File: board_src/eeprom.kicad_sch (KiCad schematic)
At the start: 4 parts, among them IC2 M93C46-WMN6TP, U2 AT24CS04-SSHM

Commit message: Wersja początkowa 9.0
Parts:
- removed IC2: M93C46-WMN6TP, SOIC127P600X175-8N, symbol M93C46-WMN6TP:M93C46-WMN6TP
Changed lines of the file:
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@@
-	)
-	(symbol
-		(lib_id "M93C46-WMN6TP:M93C46-WMN6TP")
-		(at 138.43 91.44 0)
-		(unit 1)
-		(exclude_from_sim no)
-		(in_bom yes)
-		(on_board yes)
-		(dnp no)
-		(fields_autoplaced yes)
-		(property "Reference" "IC2"
-			(at 149.86 83.82 0)
-			(effects
-				(font
-					(size 1.27 1.27)
-				)
-			)
-		)
-		(property "Value" "M93C46-WMN6TP"
-			(at 149.86 86.36 0)
-			(effects
-				(font
-					(size 1.27 1.27)
-				)
-			)
-		)
-		(property "Footprint" "SOIC127P600X175-8N"
-			(at 157.48 186.36 0)
-			(effects
-				(font
-					(size 1.27 1.27)
-				)
-				(justify left top)
-				(hide yes)
-			)
-		)
-		(property "Datasheet" "http://www.st.com/st-web-ui/static/active/en/resource/technical/document/datasheet/CD00001142.pdf"
-			(at 157.48 286.36 0)
-			(effects
-				(font
-					(size 1.27 1.27)
-				)
-				(justify left top)
-				(hide yes)
-			)
-		)
-		(property "Description" "M93C46-WMN6TP, Serial EEPROM Memory 1kbit, Serial-Microwire, 200ns 2.5  5.5 V, 8-Pin SOIC"
-			(at 138.43 91.44 0)
-			(effects
-				(font
-					(size 1.27 1.27)
-				)
-				(hide yes)
-			)
-		)
-		(property "Height" "1.75"
-			(at 157.48 486.36 0)
-			(effects
-				(font
-					(size 1.27 1.27)
-				)
-				(justify left top)
-				(hide yes)
-			)
-		)
-		(property "TME Electronic Components Part Number" ""
-			(at 157.48 586.36 0)
-			(effects
-				(font
-					(size 1.27 1.27)
-				)
-				(justify left top)
-				(hide yes)
-			)
-		)
-		(property "TME Electronic Components Price/Stock" ""
-			(at 157.48 686.36 0)
-			(effects
-				(font
-					(size 1.27 1.27)
-				)
-				(justify left top)
-				(hide yes)
-			)
-		)
-		(property "Manufacturer_Name" "STMicroelectronics"
-			(at 157.48 786.36 0)
-			(effects
-				(font
-					(size 1.27 1.27)
-				)
-				(justify left top)
-				(hide yes)
-			)
-		)
-		(property "Manufacturer_Part_Number" "M93C46-WMN6TP"
-			(at 157.48 886.36 0)
-			(effects
-				(font
-					(size 1.27 1.27)
-				)
-				(justify left top)
-				(hide yes)
-			)
-		)
-		(pin "5"
-		)
-		(pin "8"
-		)
-		(pin "2"
-		)
-		(pin "3"
-		)
-		(pin "1"
-		)
-		(pin "6"
-		)
-		(pin "7"
-		)
-		(pin "4"
-		)
-		(instances
-			(project "board"
-				(path "/772e9f49-cfcf-4cf6-843d-0684684f2d4b/8b8e205f-8cd6-4f90-881c-a100662c7649"
-					(reference "IC2")
-					(unit 1)
-				)
-			)
-		)
 	)
 	(symbol

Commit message: wersja dodane arkusze hierarchiczne
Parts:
- removed R1, R2: 10k, Resistor_SMD:R_0201_0603Metric, symbol Device:R
- removed U2: AT24CS04-SSHM, Package_SO:SOIC-8_3.9x4.9mm_P1.27mm, symbol Memory_EEPROM:AT24CS04-SSHM
- added IC2: M24C02-WMN6TP, SOIC127P600X175-8N, symbol M24C02-WMN6TP:M24C02-WMN6TP
- added J10: Conn_01x01_Pin, symbol Connector:Conn_01x01_Pin
- added R15, R16: 10k, Resistor_SMD:R_0201_0603Metric, symbol Device:R
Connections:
- new net: IC2.6 (SCL), R15.1
- new net: IC2.7 (~{WC}), J10.1 (Pin_1)
- new net: IC2.5 (SDA), R16.1
- new net 3,3V: IC2.8 (VCC), R15.2, R16.2
- new net gnd: IC2.1 (E0), IC2.2 (E1), IC2.3 (E2), IC2.4 (VSS)
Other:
- note added: "czy chcemy mieć możliwość zapisu do eeprom?"
- note removed: "EEPROM"

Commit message: wersja dodane arkusze hierarchiczne
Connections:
- net 3,3V renamed +3.3V
- net gnd renamed GND
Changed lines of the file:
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@@
-	)
-	(junction
-		(at 180.34 92.71)
-		(diameter 0)
-		(color 0 0 0 0)
 	)
 	(junction
@@
 	(wire
 		(pts
-			(xy 176.53 92.71) (xy 180.34 92.71)
+			(xy 180.34 92.71) (xy 187.96 92.71)
 		)
 		(stroke
@@
 	(wire
 		(pts
-			(xy 208.28 97.79) (xy 213.36 97.79)
+			(xy 208.28 97.79) (xy 214.63 97.79)
 		)
 		(stroke
@@
 	(wire
 		(pts
-			(xy 147.32 114.3) (xy 149.86 114.3)
-		)
-		(stroke
-			(width 0)
-			(type default)
-		)
-	)
-	(wire
-		(pts
 			(xy 200.66 97.79) (xy 208.28 97.79)
 		)
@@
 	(wire
 		(pts
-			(xy 180.34 92.71) (xy 187.96 92.71)
-		)
-		(stroke
-			(width 0)
-			(type default)
-		)
-	)
-	(wire
-		(pts
 			(xy 149.86 92.71) (xy 154.94 92.71)
 		)
@@
 		)
 	)
-	(global_label "gnd"
-		(shape passive)
-		(at 147.32 114.3 180)
+	(symbol
+		(lib_id "power:GND")
+		(at 149.86 114.3 0)
+		(unit 1)
+		(exclude_from_sim no)
+		(in_bom yes)
+		(on_board yes)
+		(dnp no)
 		(fields_autoplaced yes)
-		(effects
-			(font
-				(size 1.27 1.27)
-			)
-			(justify right)
-		)
-		(property "Intersheetrefs" "${INTERSHEET_REFS}"
-			(at 141.9991 114.3 0)
-			(effects
-				(font
-					(size 1.27 1.27)
-				)
-				(justify right)
-				(hide yes)
-			)
-		)
-	)
-	(global_label "3,3V"
-		(shape passive)
-		(at 213.36 97.79 0)
-		(fields_autoplaced yes)
-		(effects
-			(font
-				(size 1.27 1.27)
-			)
-			(justify left)
-		)
-		(property "Intersheetrefs" "${INTERSHEET_REFS}"
-			(at 219.3463 97.79 0)
-			(effects
-				(font
-					(size 1.27 1.27)
-				)
-				(justify left)
-				(hide yes)
+		(property "Reference" "#PWR017"
+			(at 149.86 120.65 0)
+			(effects
+				(font
+					(size 1.27 1.27)
+				)
+				(hide yes)
+			)
+		)
+		(property "Value" "GND"
+			(at 149.86 119.38 0)
+			(effects
+				(font
+					(size 1.27 1.27)
+				)
+			)
+		)
+		(property "Footprint" ""
+			(at 149.86 114.3 0)
+			(effects
+				(font
+					(size 1.27 1.27)
+				)
+				(hide yes)
+			)
+		)
+		(property "Datasheet" ""
+			(at 149.86 114.3 0)
+			(effects
+				(font
+					(size 1.27 1.27)
+				)
+				(hide yes)
+			)
+		)
+		(property "Description" "Power symbol creates a global label with name \"GND\" , ground"
+			(at 149.86 114.3 0)
+			(effects
+				(font
+					(size 1.27 1.27)
+				)
+				(hide yes)
+			)
+		)
+		(pin "1"
+		)
+		(instances
+			(project ""
+				(path "/772e9f49-cfcf-4cf6-843d-0684684f2d4b/8b8e205f-8cd6-4f90-881c-a100662c7649"
+					(reference "#PWR017")
+					(unit 1)
+				)
 			)
 		)
@@
 					(unit 1)
 				)
+			)
+		)
+	)
+	(symbol
+		(lib_id "power:+3.3V")
+		(at 214.63 97.79 270)
+		(unit 1)
+		(exclude_from_sim no)
+		(in_bom yes)
+		(on_board yes)
+		(dnp no)
+		(fields_autoplaced yes)
+		(property "Reference" "#PWR010"
+			(at 210.82 97.79 0)
+			(effects
+				(font
+					(size 1.27 1.27)
+				)
+				(hide yes)
+			)
+		)
+		(property "Value" "+3.3V"
+			(at 218.44 97.7899 90)
+			(effects
+				(font
+					(size 1.27 1.27)
+				)
+				(justify left)
+			)
+		)
+		(property "Footprint" ""
+			(at 214.63 97.79 0)
+			(effects
+				(font
+					(size 1.27 1.27)
+				)
+				(hide yes)
+			)
+		)
+		(property "Datasheet" ""
+			(at 214.63 97.79 0)
+			(effects
+				(font
+					(size 1.27 1.27)
+				)
+				(hide yes)
+			)
+		)
+		(property "Description" "Power symbol creates a global label with name \"+3.3V\""
+			(at 214.63 97.79 0)
+			(effects
+				(font
+					(size 1.27 1.27)
+				)
+				(hide yes)
+			)
+		)
+		(pin "1"
+		)
+		(instances
+			(project "board"
+				(path "/772e9f49-cfcf-4cf6-843d-0684684f2d4b/8b8e205f-8cd6-4f90-881c-a100662c7649"
+					(reference "#PWR010")
+					(unit 1)
+				)

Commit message: wersja uzupelnione footprinty
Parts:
- IC2: footprint SOIC127P600X175-8N -> footprints:EEPROM
- J10: footprint (none) -> Connector_PinHeader_2.54mm:PinHeader_1x01_P2.54mm_Vertical
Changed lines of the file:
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@@
 			)
 		)
-		(property "Footprint" ""
+		(property "Footprint" "Connector_PinHeader_2.54mm:PinHeader_1x01_P2.54mm_Vertical"
 			(at 193.04 92.71 0)
 			(effects
@@
 			)
 		)
-		(property "Footprint" "SOIC127P600X175-8N"
+		(property "Footprint" "footprints:EEPROM"
 			(at 176.53 185.09 0)
 			(effects

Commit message: wersja 3d
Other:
- note added: "Jaka wartość oporników?"
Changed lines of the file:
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@@
 	(generator_version "9.0")
 	(paper "A4")
+	(text "Jaka wartość oporników?\n"
+		(exclude_from_sim no)
+		(at 193.548 113.284 0)
+		(effects
+			(font
+				(size 1.27 1.27)
+			)
+		)
+	)
 	(text "czy chcemy mieć możliwość zapisu do eeprom?"
 		(exclude_from_sim no)

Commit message: uporzadkowane 3D
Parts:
- added J19, J28: Conn_01x01_Pin, Connector_PinHeader_2.54mm:PinHeader_1x01_P2.54mm_Vertical, symbol Connector:Conn_01x01_Pin
- R15, R16: value 10k -> 4.7k
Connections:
- net +3.3V: no longer R15.2, R16.2
- new net: J28.1 (Pin_1), R16.2
- new net: J19.1 (Pin_1), R15.2
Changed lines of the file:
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@@
-	)
-	(junction
-		(at 208.28 97.79)
-		(diameter 0)
-		(color 0 0 0 0)
 	)
 	(junction
@@
 		(color 0 0 0 0)
 	)
-	(junction
-		(at 200.66 97.79)
-		(diameter 0)
-		(color 0 0 0 0)
+	(wire
+		(pts
+			(xy 205.74 102.87) (xy 205.74 100.33)
+		)
+		(stroke
+			(width 0)
+			(type default)
+		)
 	)
 	(wire
@@
 	(wire
 		(pts
-			(xy 196.85 97.79) (xy 200.66 97.79)
-		)
-		(stroke
-			(width 0)
-			(type default)
-		)
-	)
-	(wire
-		(pts
 			(xy 149.86 92.71) (xy 149.86 95.25)
 		)
@@
 	(wire
 		(pts
-			(xy 185.42 85.09) (xy 208.28 85.09)
+			(xy 185.42 85.09) (xy 214.63 85.09)
 		)
 		(stroke
@@
 	(wire
 		(pts
-			(xy 208.28 97.79) (xy 214.63 97.79)
-		)
-		(stroke
-			(width 0)
-			(type default)
-		)
-	)
-	(wire
-		(pts
 			(xy 149.86 97.79) (xy 149.86 114.3)
 		)
@@
 	(wire
 		(pts
-			(xy 196.85 97.79) (xy 196.85 102.87)
-		)
-		(stroke
-			(width 0)
-			(type default)
-		)
-	)
-	(wire
-		(pts
-			(xy 200.66 97.79) (xy 208.28 97.79)
+			(xy 196.85 102.87) (xy 205.74 102.87)
 		)
 		(stroke
@@
 	(wire
 		(pts
-			(xy 196.85 105.41) (xy 200.66 105.41)
-		)
-		(stroke
-			(width 0)
-			(type default)
-		)
-	)
-	(wire
-		(pts
-			(xy 200.66 97.79) (xy 200.66 105.41)
-		)
-		(stroke
-			(width 0)
-			(type default)
-		)
-	)
-	(wire
-		(pts
-			(xy 208.28 85.09) (xy 208.28 97.79)
+			(xy 196.85 105.41) (xy 205.74 105.41)
 		)
 		(stroke
@@
 		(pts
 			(xy 149.86 90.17) (xy 149.86 92.71)
+		)
+		(stroke
+			(width 0)
+			(type default)
+		)
+	)
+	(wire
+		(pts
+			(xy 205.74 105.41) (xy 205.74 106.68)
 		)
 		(stroke
@@
 	)
 	(symbol
+		(lib_id "Connector:Conn_01x01_Pin")
+		(at 210.82 106.68 180)
+		(unit 1)
+		(exclude_from_sim no)
+		(in_bom yes)
+		(on_board yes)
+		(dnp no)
+		(property "Reference" "J28"
+			(at 211.074 104.902 0)
+			(effects
+				(font
+					(size 1.27 1.27)
+				)
+			)
+		)
+		(property "Value" "Conn_01x01_Pin"
+			(at 219.964 106.426 0)
+			(effects
+				(font
+					(size 1.27 1.27)
+				)
+			)
+		)
+		(property "Footprint" "Connector_PinHeader_2.54mm:PinHeader_1x01_P2.54mm_Vertical"
+			(at 210.82 106.68 0)
+			(effects
+				(font
+					(size 1.27 1.27)
+				)
+				(hide yes)
+			)
+		)
+		(property "Datasheet" "~"
+			(at 210.82 106.68 0)
+			(effects
+				(font
+					(size 1.27 1.27)
+				)
+				(hide yes)
+			)
+		)
+		(property "Description" "Generic connector, single row, 01x01, script generated"
+			(at 210.82 106.68 0)
+			(effects
+				(font
+					(size 1.27 1.27)
+				)
+				(hide yes)
+			)
+		)
+		(pin "1"
+		)
+		(instances
+			(project "board"
+				(path "/772e9f49-cfcf-4cf6-843d-0684684f2d4b/8b8e205f-8cd6-4f90-881c-a100662c7649"
+					(reference "J28")
+					(unit 1)
+				)
+			)
+		)
+	)
+	(symbol
 		(lib_id "Device:R")
 		(at 193.04 102.87 90)
@@
 			)
 		)
-		(property "Value" "10k"
+		(property "Value" "4.7k"
 			(at 193.04 99.06 90)
 			(effects
@@
 	(symbol
 		(lib_id "power:+3.3V")
-		(at 214.63 97.79 270)
+		(at 214.63 85.09 270)
 		(unit 1)
 		(exclude_from_sim no)
@@
 		(on_board yes)
 		(dnp no)
-		(fields_autoplaced yes)
 		(property "Reference" "#PWR010"
-			(at 210.82 97.79 0)
+			(at 210.82 85.09 0)
 			(effects
 				(font
@@
 		)
 		(property "Value" "+3.3V"
-			(at 218.44 97.7899 90)
+			(at 217.678 85.09 90)
 			(effects
 				(font
@@
 		)
 		(property "Footprint" ""
-			(at 214.63 97.79 0)
+			(at 214.63 85.09 0)
 			(effects
 				(font
@@
 		)
 		(property "Datasheet" ""
-			(at 214.63 97.79 0)
+			(at 214.63 85.09 0)
 			(effects
 				(font
@@
 		)
 		(property "Description" "Power symbol creates a global label with name \"+3.3V\""
-			(at 214.63 97.79 0)
+			(at 214.63 85.09 0)
 			(effects
 				(font
@@
 				(path "/772e9f49-cfcf-4cf6-843d-0684684f2d4b/8b8e205f-8cd6-4f90-881c-a100662c7649"
 					(reference "J10")
+					(unit 1)
+				)
+			)
+		)
+	)
+	(symbol
+		(lib_id "Connector:Conn_01x01_Pin")
+		(at 210.82 100.33 180)
+		(unit 1)
+		(exclude_from_sim no)
+		(in_bom yes)
+		(on_board yes)
+		(dnp no)
+		(property "Reference" "J19"
+			(at 211.328 99.06 0)
+			(effects
+				(font
+					(size 1.27 1.27)
+				)
+			)
+		)
+		(property "Value" "Conn_01x01_Pin"
+			(at 220.726 100.33 0)
+			(effects
+				(font
+					(size 1.27 1.27)
+				)
+			)
+		)
+		(property "Footprint" "Connector_PinHeader_2.54mm:PinHeader_1x01_P2.54mm_Vertical"
+			(at 210.82 100.33 0)
+			(effects
+				(font
+					(size 1.27 1.27)
+				)
+				(hide yes)
+			)
+		)
+		(property "Datasheet" "~"
+			(at 210.82 100.33 0)
+			(effects
+				(font
+					(size 1.27 1.27)
+				)
+				(hide yes)
+			)
+		)
+		(property "Description" "Generic connector, single row, 01x01, script generated"
+			(at 210.82 100.33 0)
+			(effects
+				(font
+					(size 1.27 1.27)
+				)
+				(hide yes)
+			)
+		)
+		(pin "1"
+		)
+		(instances
+			(project ""
+				(path "/772e9f49-cfcf-4cf6-843d-0684684f2d4b/8b8e205f-8cd6-4f90-881c-a100662c7649"
+					(reference "J19")
 					(unit 1)
 				)
@@
 			)
 		)
-		(property "Value" "10k"
+		(property "Value" "4.7k"
 			(at 193.04 109.474 90)
 			(effects

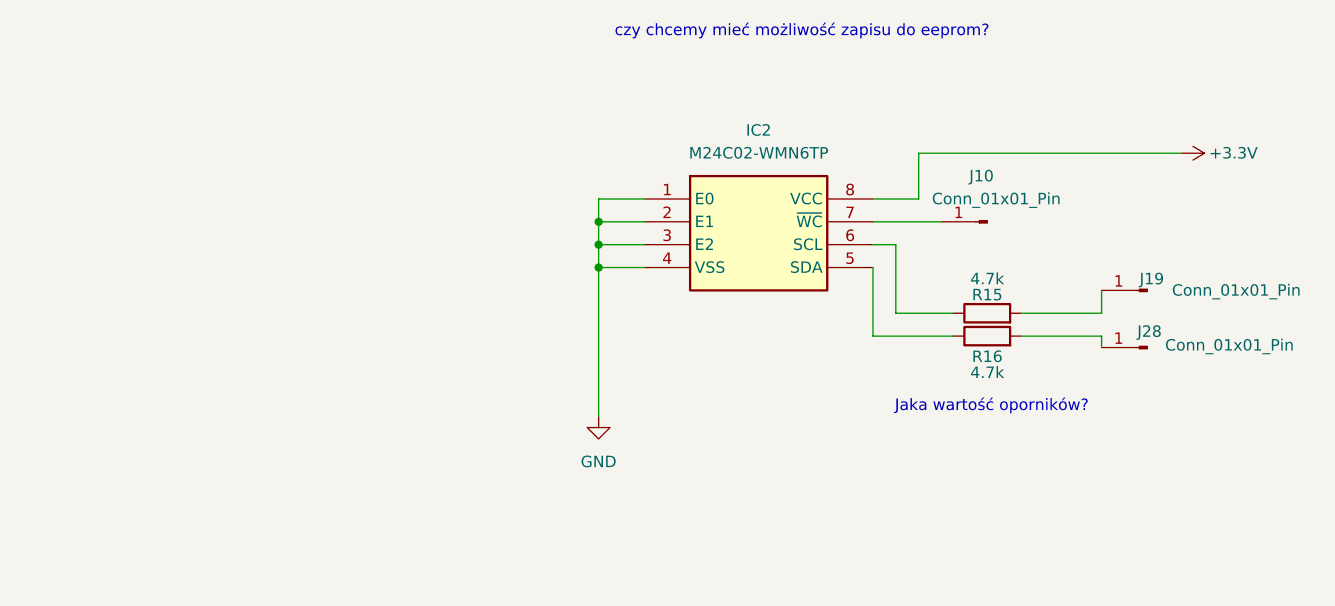
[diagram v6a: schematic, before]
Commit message: wersja z wyswietlaczem LCD
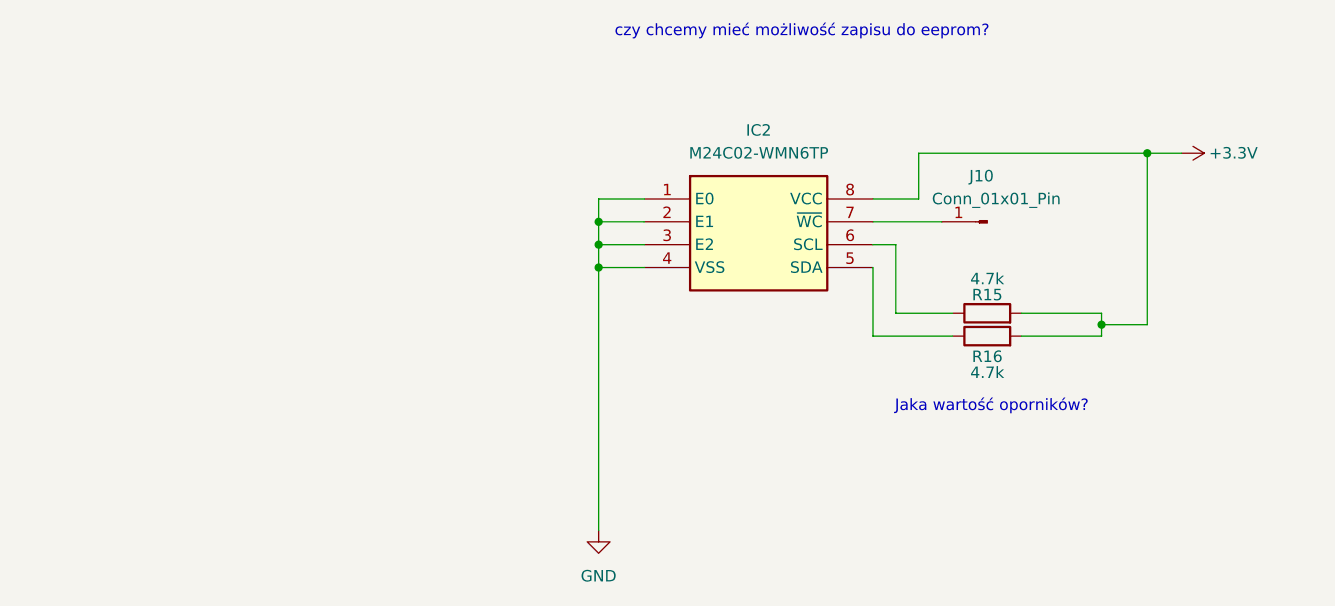
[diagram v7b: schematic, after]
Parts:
- removed J19, J28: Conn_01x01_Pin, Connector_PinHeader_2.54mm:PinHeader_1x01_P2.54mm_Vertical, symbol Connector:Conn_01x01_Pin
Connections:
- net +3.3V: now also R15.2, R16.2
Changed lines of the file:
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@@
+	)
+	(junction
+		(at 205.74 104.14)
+		(diameter 0)
+		(color 0 0 0 0)
 	)
 	(junction
@@
 		(color 0 0 0 0)
 	)
-	(wire
-		(pts
-			(xy 205.74 102.87) (xy 205.74 100.33)
-		)
-		(stroke
-			(width 0)
-			(type default)
-		)
+	(junction
+		(at 210.82 85.09)
+		(diameter 0)
+		(color 0 0 0 0)
 	)
 	(wire
@@
 	(wire
 		(pts
+			(xy 205.74 104.14) (xy 210.82 104.14)
+		)
+		(stroke
+			(width 0)
+			(type default)
+		)
+	)
+	(wire
+		(pts
+			(xy 210.82 104.14) (xy 210.82 85.09)
+		)
+		(stroke
+			(width 0)
+			(type default)
+		)
+	)
+	(wire
+		(pts
+			(xy 205.74 102.87) (xy 205.74 104.14)
+		)
+		(stroke
+			(width 0)
+			(type default)
+		)
+	)
+	(wire
+		(pts
 			(xy 149.86 92.71) (xy 149.86 95.25)
 		)
@@
 	(wire
 		(pts
-			(xy 185.42 85.09) (xy 214.63 85.09)
+			(xy 185.42 85.09) (xy 210.82 85.09)
 		)
 		(stroke
@@
 	(wire
 		(pts
-			(xy 149.86 97.79) (xy 149.86 114.3)
+			(xy 149.86 97.79) (xy 149.86 127)
 		)
 		(stroke
@@
 	(wire
 		(pts
+			(xy 205.74 104.14) (xy 205.74 105.41)
+		)
+		(stroke
+			(width 0)
+			(type default)
+		)
+	)
+	(wire
+		(pts
 			(xy 182.88 102.87) (xy 189.23 102.87)
 		)
@@
 	(wire
 		(pts
+			(xy 210.82 85.09) (xy 214.63 85.09)
+		)
+		(stroke
+			(width 0)
+			(type default)
+		)
+	)
+	(wire
+		(pts
 			(xy 196.85 105.41) (xy 205.74 105.41)
 		)
@@
 		(pts
 			(xy 149.86 90.17) (xy 149.86 92.71)
-		)
-		(stroke
-			(width 0)
-			(type default)
-		)
-	)
-	(wire
-		(pts
-			(xy 205.74 105.41) (xy 205.74 106.68)
 		)
 		(stroke
@@
 	(symbol
 		(lib_id "power:GND")
-		(at 149.86 114.3 0)
+		(at 149.86 127 0)
 		(unit 1)
 		(exclude_from_sim no)
@@
 		(fields_autoplaced yes)
 		(property "Reference" "#PWR017"
-			(at 149.86 120.65 0)
+			(at 149.86 133.35 0)
 			(effects
 				(font
@@
 		)
 		(property "Value" "GND"
-			(at 149.86 119.38 0)
+			(at 149.86 132.08 0)
 			(effects
 				(font
@@
 		)
 		(property "Footprint" ""
-			(at 149.86 114.3 0)
+			(at 149.86 127 0)
 			(effects
 				(font
@@
 		)
 		(property "Datasheet" ""
-			(at 149.86 114.3 0)
+			(at 149.86 127 0)
 			(effects
 				(font
@@
 		)
 		(property "Description" "Power symbol creates a global label with name \"GND\" , ground"
-			(at 149.86 114.3 0)
+			(at 149.86 127 0)
 			(effects
 				(font
@@
 				(path "/772e9f49-cfcf-4cf6-843d-0684684f2d4b/8b8e205f-8cd6-4f90-881c-a100662c7649"
 					(reference "#PWR017")
-					(unit 1)
-				)
-			)
-		)
-	)
-	(symbol
-		(lib_id "Connector:Conn_01x01_Pin")
-		(at 210.82 106.68 180)
-		(unit 1)
-		(exclude_from_sim no)
-		(in_bom yes)
-		(on_board yes)
-		(dnp no)
-		(property "Reference" "J28"
-			(at 211.074 104.902 0)
-			(effects
-				(font
-					(size 1.27 1.27)
-				)
-			)
-		)
-		(property "Value" "Conn_01x01_Pin"
-			(at 219.964 106.426 0)
-			(effects
-				(font
-					(size 1.27 1.27)
-				)
-			)
-		)
-		(property "Footprint" "Connector_PinHeader_2.54mm:PinHeader_1x01_P2.54mm_Vertical"
-			(at 210.82 106.68 0)
-			(effects
-				(font
-					(size 1.27 1.27)
-				)
-				(hide yes)
-			)
-		)
-		(property "Datasheet" "~"
-			(at 210.82 106.68 0)
-			(effects
-				(font
-					(size 1.27 1.27)
-				)
-				(hide yes)
-			)
-		)
-		(property "Description" "Generic connector, single row, 01x01, script generated"
-			(at 210.82 106.68 0)
-			(effects
-				(font
-					(size 1.27 1.27)
-				)
-				(hide yes)
-			)
-		)
-		(pin "1"
-		)
-		(instances
-			(project "board"
-				(path "/772e9f49-cfcf-4cf6-843d-0684684f2d4b/8b8e205f-8cd6-4f90-881c-a100662c7649"
-					(reference "J28")
 					(unit 1)
 				)
@@
 					(unit 1)
 				)
-			)
-		)
-	)
-	(symbol
-		(lib_id "Connector:Conn_01x01_Pin")
-		(at 210.82 100.33 180)
-		(unit 1)
-		(exclude_from_sim no)
-		(in_bom yes)
-		(on_board yes)
-		(dnp no)
-		(property "Reference" "J19"
-			(at 211.328 99.06 0)
-			(effects
-				(font
-					(size 1.27 1.27)
-				)
-			)
-		)
-		(property "Value" "Conn_01x01_Pin"
-			(at 220.726 100.33 0)
-			(effects
-				(font
-					(size 1.27 1.27)
-				)
-			)
-		)
-		(property "Footprint" "Connector_PinHeader_2.54mm:PinHeader_1x01_P2.54mm_Vertical"
-			(at 210.82 100.33 0)
-			(effects
-				(font
-					(size 1.27 1.27)
-				)
-				(hide yes)
-			)
-		)
-		(property "Datasheet" "~"
-			(at 210.82 100.33 0)
-			(effects
-				(font
-					(size 1.27 1.27)
-				)
-				(hide yes)
-			)
-		)
-		(property "Description" "Generic connector, single row, 01x01, script generated"
-			(at 210.82 100.33 0)
-			(effects
-				(font
-					(size 1.27 1.27)
-				)
-				(hide yes)
-			)
-		)
-		(pin "1"
-		)
-		(instances
-			(project ""
-				(path "/772e9f49-cfcf-4cf6-843d-0684684f2d4b/8b8e205f-8cd6-4f90-881c-a100662c7649"
-					(reference "J19")
-					(unit 1)
-				)

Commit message: wersja z FT232RN
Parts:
- removed J10: Conn_01x01_Pin, Connector_PinHeader_2.54mm:PinHeader_1x01_P2.54mm_Vertical, symbol Connector:Conn_01x01_Pin
- added J6: Conn_01x02_Pin, Connector_PinHeader_2.54mm:PinHeader_1x02_P2.54mm_Vertical, symbol Connector:Conn_01x02_Pin
- added J8: Conn_01x01_Pin, Connector_PinHeader_2.54mm:PinHeader_1x01_P2.54mm_Vertical, symbol Connector:Conn_01x01_Pin
- R15, R16: footprint Resistor_SMD:R_0201_0603Metric -> Resistor_SMD:R_1206_3216Metric
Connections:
- net GND: now also IC2.7 (~{WC}), J8.1 (Pin_1)
- net at IC2.6 (SCL), R15.1: now also J6.2 (Pin_2)
- net at IC2.5 (SDA), R16.1: now also J6.1 (Pin_1)
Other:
- note removed: "Jaka wartość oporników?"
- moved on the sheet: R15, R16
